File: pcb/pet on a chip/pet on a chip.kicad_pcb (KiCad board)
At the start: 4 copper layers, 76.2 x 63.5 mm, 69 parts, among them J1 USB_B, J2 Screw_Terminal_01x02, J3 Conn_02x15_Odd_Even, J4 Conn_02x15_Odd_Even, SW1 SW_Push, SW2 SW_Push, U1 93LCxxC, U2 FT2232HL, U3 LDL1117S33R, U4 TLV70012DDCR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

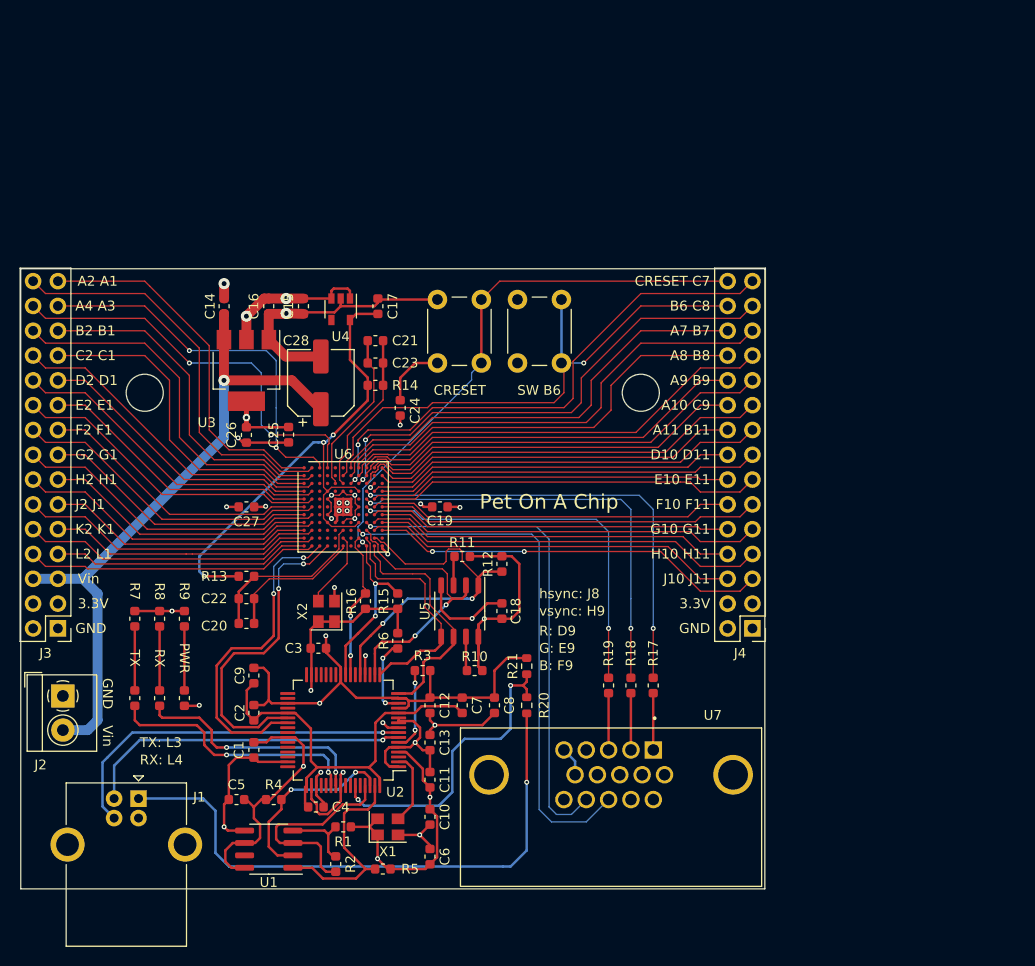
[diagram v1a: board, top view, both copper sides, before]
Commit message: cleaned up pcb location
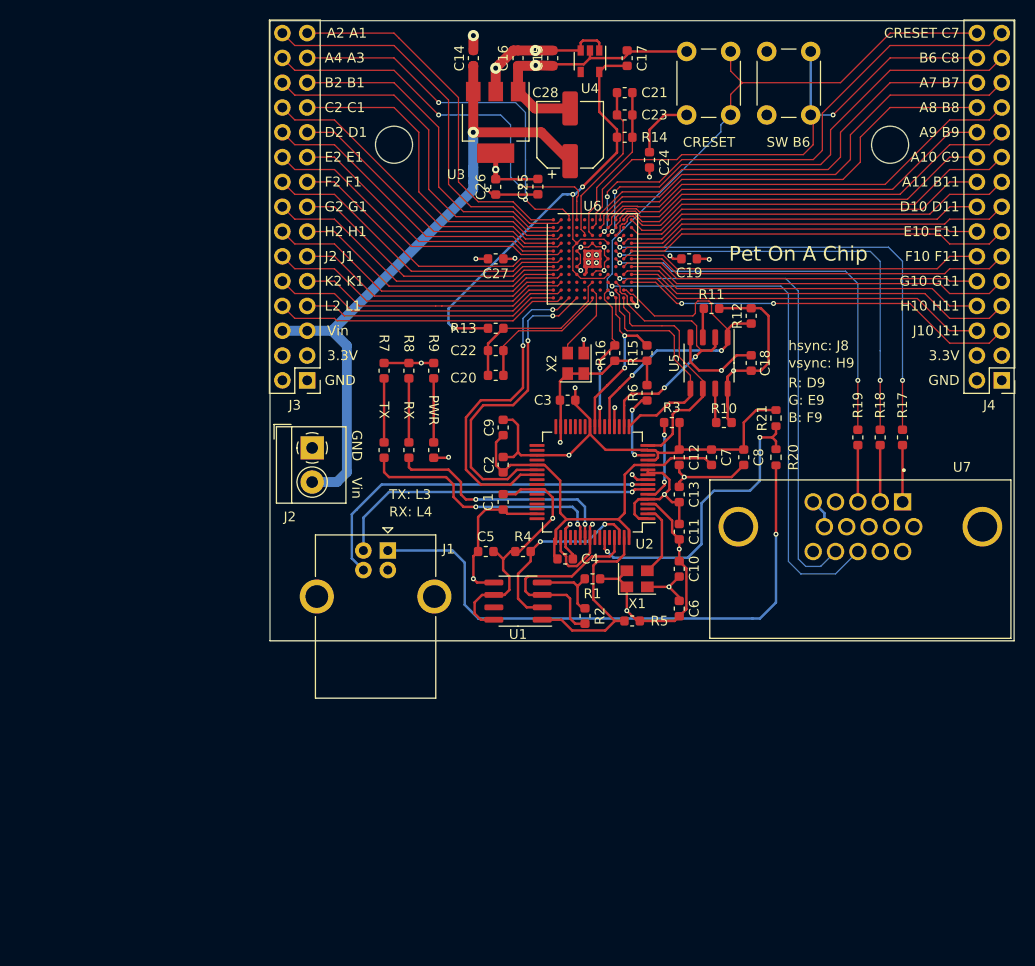
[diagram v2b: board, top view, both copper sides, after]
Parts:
- moved C8 36.0 mm to (150.2, 108.2)
- moved R2 36.0 mm to (134.0, 124.5)
- moved R20 36.0 mm to (153.5, 108.2)
- moved C12 36.0 mm to (143.6, 108.2)
- moved C2 36.0 mm to (125.6, 109.0)
- moved C28 36.0 mm to (132.5, 75.2)
- moved C6 36.0 mm to (143.6, 123.7)
- moved J4 36.0 mm to (176.7, 100.3)
- moved R1 36.0 mm to (134.7, 120.7)
- moved R17 36.0 mm to (166.5, 106.2)
- moved R18 36.0 mm to (164.2, 106.2)
- moved R19 36.0 mm to (161.9, 106.2)
- moved U2 36.0 mm to (134.7, 110.7)
- moved U6 36.0 mm to (134.7, 87.9)
- moved U7 36.0 mm to (162.2, 115.3)
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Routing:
- net CRESET: track 74.4 -> 75.5 mm
